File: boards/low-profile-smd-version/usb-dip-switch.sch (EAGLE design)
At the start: 19 parts, among them SW1 KMR211NGLFS, SW2 219-08, U1 PIC16F1459-I/SS, U2 PRTR5V0U2X

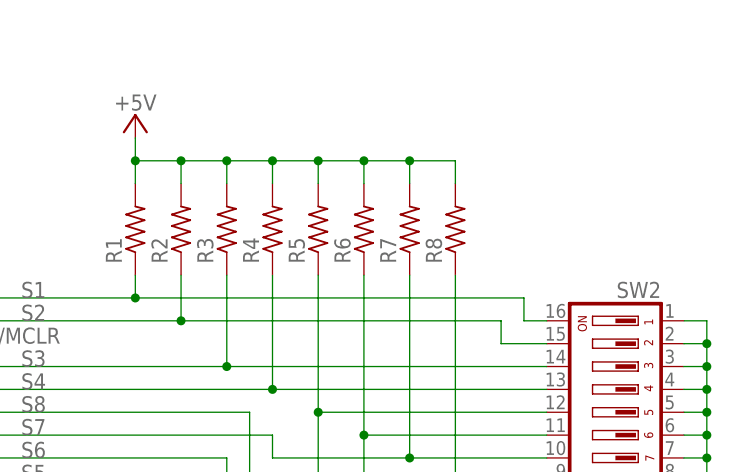
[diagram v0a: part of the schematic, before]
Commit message: add 100k value to pullup resistors R1-R8
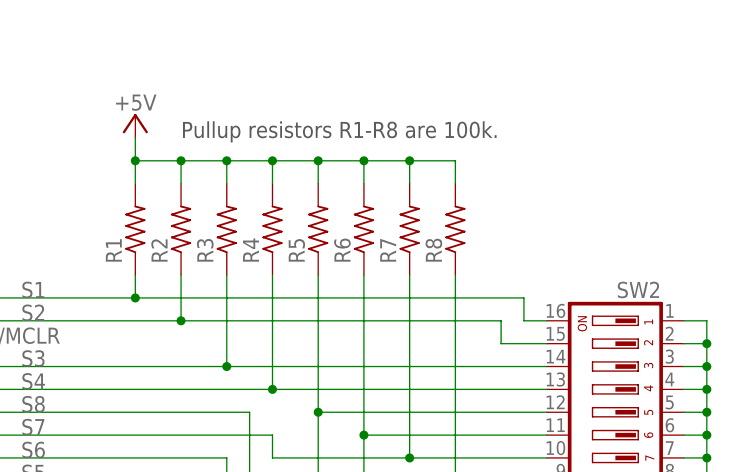
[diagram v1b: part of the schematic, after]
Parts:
- R1, R2, R3, R4, R5, R6, R7, R8: value (none) -> 100k
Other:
- note added: "Pullup resistors R1-R8 are 100k."
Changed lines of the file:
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@@
 <part name="SW2" library="switch-dil" deviceset="219-08*" device=""/>
 <part name="SUPPLY7" library="supply2" deviceset="GND" device=""/>
-<part name="R1" library="rcl" deviceset="R-US_" device="R0603"/>
-<part name="R2" library="rcl" deviceset="R-US_" device="R0603"/>
-<part name="R3" library="rcl" deviceset="R-US_" device="R0603"/>
-<part name="R4" library="rcl" deviceset="R-US_" device="R0603"/>
-<part name="R5" library="rcl" deviceset="R-US_" device="R0603"/>
-<part name="R6" library="rcl" deviceset="R-US_" device="R0603"/>
-<part name="R7" library="rcl" deviceset="R-US_" device="R0603"/>
-<part name="R8" library="rcl" deviceset="R-US_" device="R0603"/>
+<part name="R1" library="rcl" deviceset="R-US_" device="R0603" value="100k"/>
+<part name="R2" library="rcl" deviceset="R-US_" device="R0603" value="100k"/>
+<part name="R3" library="rcl" deviceset="R-US_" device="R0603" value="100k"/>
+<part name="R4" library="rcl" deviceset="R-US_" device="R0603" value="100k"/>
+<part name="R5" library="rcl" deviceset="R-US_" device="R0603" value="100k"/>
+<part name="R6" library="rcl" deviceset="R-US_" device="R0603" value="100k"/>
+<part name="R7" library="rcl" deviceset="R-US_" device="R0603" value="100k"/>
+<part name="R8" library="rcl" deviceset="R-US_" device="R0603" value="100k"/>
 <part name="P+4" library="supply1" deviceset="+5V" device=""/>
 </parts>
@@
 <text x="215.9" y="114.3" size="1.778" layer="97" align="top-left">219-8MSTR
 CT3121CT-ND</text>
+<text x="177.8" y="162.56" size="1.778" layer="97">Pullup resistors R1-R8 are 100k.</text>
 </plain>
 <instances>
@@
 <instance part="SW2" gate="G$1" x="226.06" y="132.08" rot="MR270"/>
 <instance part="SUPPLY7" gate="GND" x="236.22" y="119.38" rot="MR0"/>
-<instance part="R1" gate="G$1" x="172.72" y="152.4" rot="R90"/>
-<instance part="R2" gate="G$1" x="177.8" y="152.4" rot="R90"/>
-<instance part="R3" gate="G$1" x="182.88" y="152.4" rot="R90"/>
-<instance part="R4" gate="G$1" x="187.96" y="152.4" rot="R90"/>
-<instance part="R5" gate="G$1" x="193.04" y="152.4" rot="R90"/>
-<instance part="R6" gate="G$1" x="198.12" y="152.4" rot="R90"/>
-<instance part="R7" gate="G$1" x="203.2" y="152.4" rot="R90"/>
-<instance part="R8" gate="G$1" x="208.28" y="152.4" rot="R90"/>
+<instance part="R1" gate="G$1" x="172.72" y="152.4" smashed="yes" rot="R90">
+<attribute name="NAME" x="171.2214" y="148.59" size="1.778" layer="95" rot="R90"/>
+</instance>
+<instance part="R2" gate="G$1" x="177.8" y="152.4" smashed="yes" rot="R90">
+<attribute name="NAME" x="176.3014" y="148.59" size="1.778" layer="95" rot="R90"/>
+</instance>
+<instance part="R3" gate="G$1" x="182.88" y="152.4" smashed="yes" rot="R90">
+<attribute name="NAME" x="181.3814" y="148.59" size="1.778" layer="95" rot="R90"/>
+</instance>
+<instance part="R4" gate="G$1" x="187.96" y="152.4" smashed="yes" rot="R90">
+<attribute name="NAME" x="186.4614" y="148.59" size="1.778" layer="95" rot="R90"/>
+</instance>
+<instance part="R5" gate="G$1" x="193.04" y="152.4" smashed="yes" rot="R90">
+<attribute name="NAME" x="191.5414" y="148.59" size="1.778" layer="95" rot="R90"/>
+</instance>
+<instance part="R6" gate="G$1" x="198.12" y="152.4" smashed="yes" rot="R90">
+<attribute name="NAME" x="196.6214" y="148.59" size="1.778" layer="95" rot="R90"/>
+</instance>
+<instance part="R7" gate="G$1" x="203.2" y="152.4" smashed="yes" rot="R90">
+<attribute name="NAME" x="201.7014" y="148.59" size="1.778" layer="95" rot="R90"/>
+</instance>
+<instance part="R8" gate="G$1" x="208.28" y="152.4" smashed="yes" rot="R90">
+<attribute name="NAME" x="206.7814" y="148.59" size="1.778" layer="95" rot="R90"/>
+</instance>
 <instance part="P+4" gate="1" x="172.72" y="165.1" smashed="yes" rot="MR0">
 <attribute name="VALUE" x="172.72" y="165.608" size="1.778" layer="96" rot="MR0" align="bottom-center"/>
